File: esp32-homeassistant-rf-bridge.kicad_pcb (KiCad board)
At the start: 2 copper layers, 52 x 51.8 mm, 37 parts, among them J1 USB_C_Receptacle_USB2.0_16P, J2 Conn_02x04_Odd_Even, SW1 SW_Push, SW2 SW_Push, SW3 SW_Push, SW4 SW_Push, U1 ESP32-S2-MINI-1, U2 TSOP41xx, U3 XC6206P332MR, U4 CC1101_E07-M1101D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

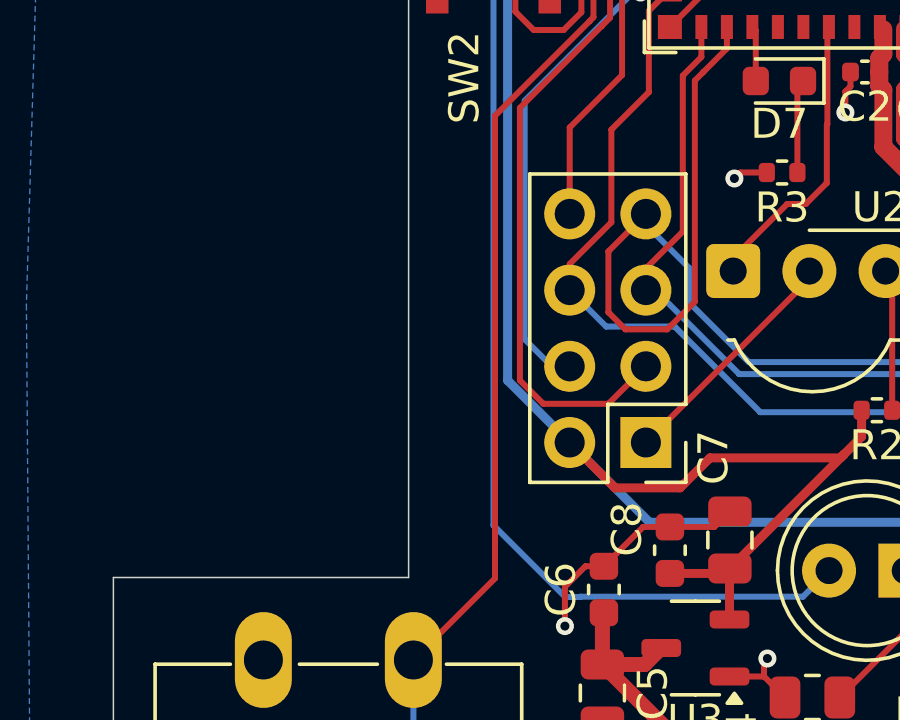
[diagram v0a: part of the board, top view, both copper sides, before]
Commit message: add JLCPCB ID designator
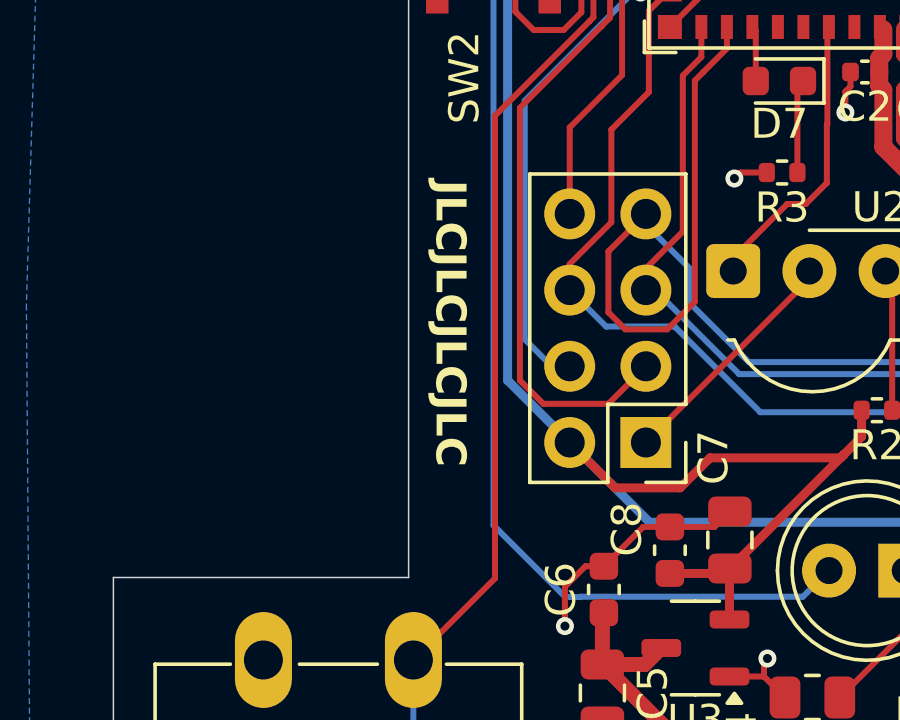
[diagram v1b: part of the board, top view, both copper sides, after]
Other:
- board text added: "JLCJLCJLCJLC"
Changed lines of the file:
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@@
 		(layer "Edge.Cuts")
+	)
+	(gr_text "JLCJLCJLCJLC"
+		(at 87.65 37.75 270)
+		(layer "F.SilkS")
+		(effects
+			(font
+				(size 1 1)
+				(thickness 0.2)
+				(bold yes)
+			)
+			(justify left bottom)
+		)
 	)
 	(gr_text "@grimsteel\n"

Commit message: silkscreen updates, add LDR and mounting holes
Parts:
- added R5: LDR07, OptoDevice:R_LDR_5.0x4.1mm_P3mm_Vertical, F.Cu at (112.0, 52.2)
- added R6: 10K, Resistor_SMD:R_0402_1005Metric, F.Cu at (109.5, 55.3)
- added REF**: MountingHole_3.2mm_M3, MountingHole:MountingHole_3.2mm_M3, F.Cu at (123.7, 48.2)
- added REF**: MountingHole_3.2mm_M3, MountingHole:MountingHole_3.2mm_M3, F.Cu at (82.2, 48.2)
- D6: value D6 -> LD271
- moved QR***** 1.01 mm to (100.5, 28.1)
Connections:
- U1 pad 32: unconnected-(U1-GPIO36-Pad32) -> LDR
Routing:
- net LDR: track 0.00 -> 34.6 mm, vias 0 -> 1
- net +3.3V: track 113.4 -> 117.7 mm
- net GND: track 105.9 -> 106.8 mm, vias 24 -> 25
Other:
- outline, holes or cut-outs redrawn
- board text added: "01/25"
- board text removed: "12/24"

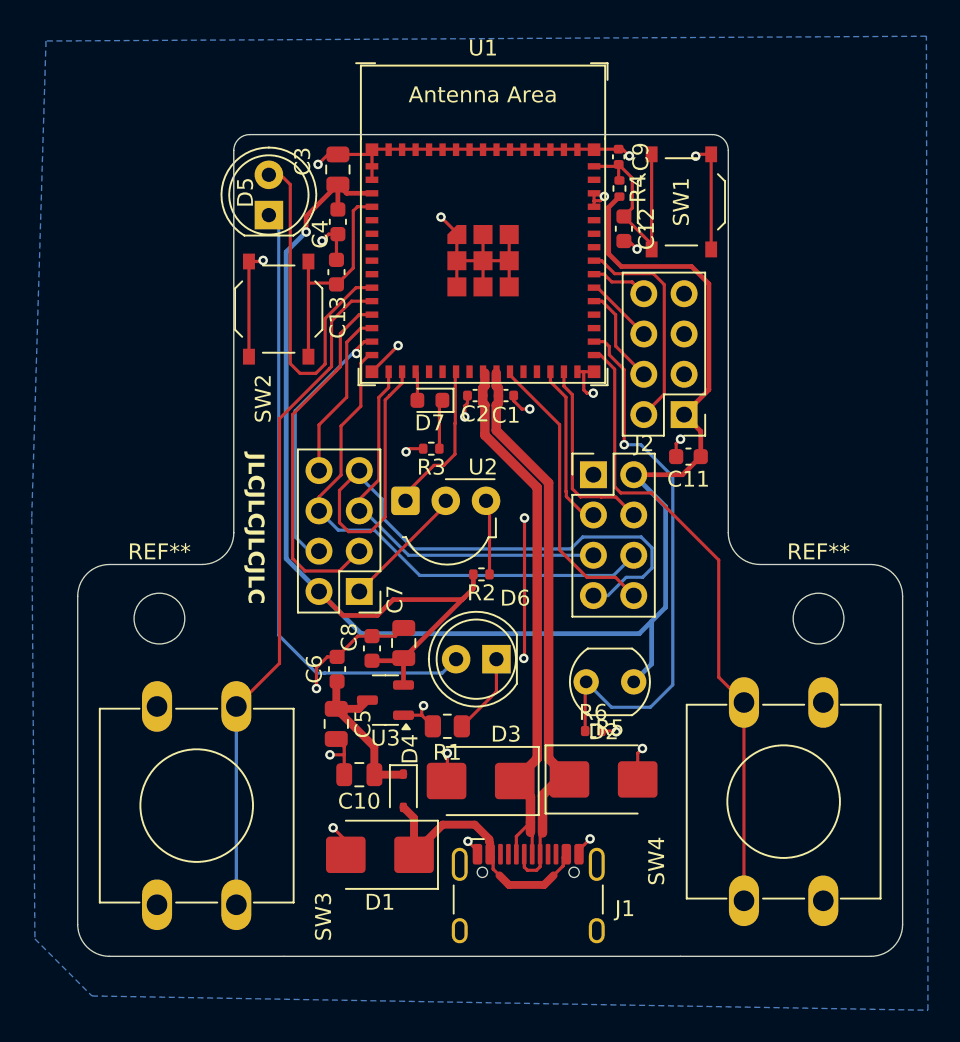
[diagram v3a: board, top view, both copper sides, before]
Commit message: make board smaller, remove problematic components
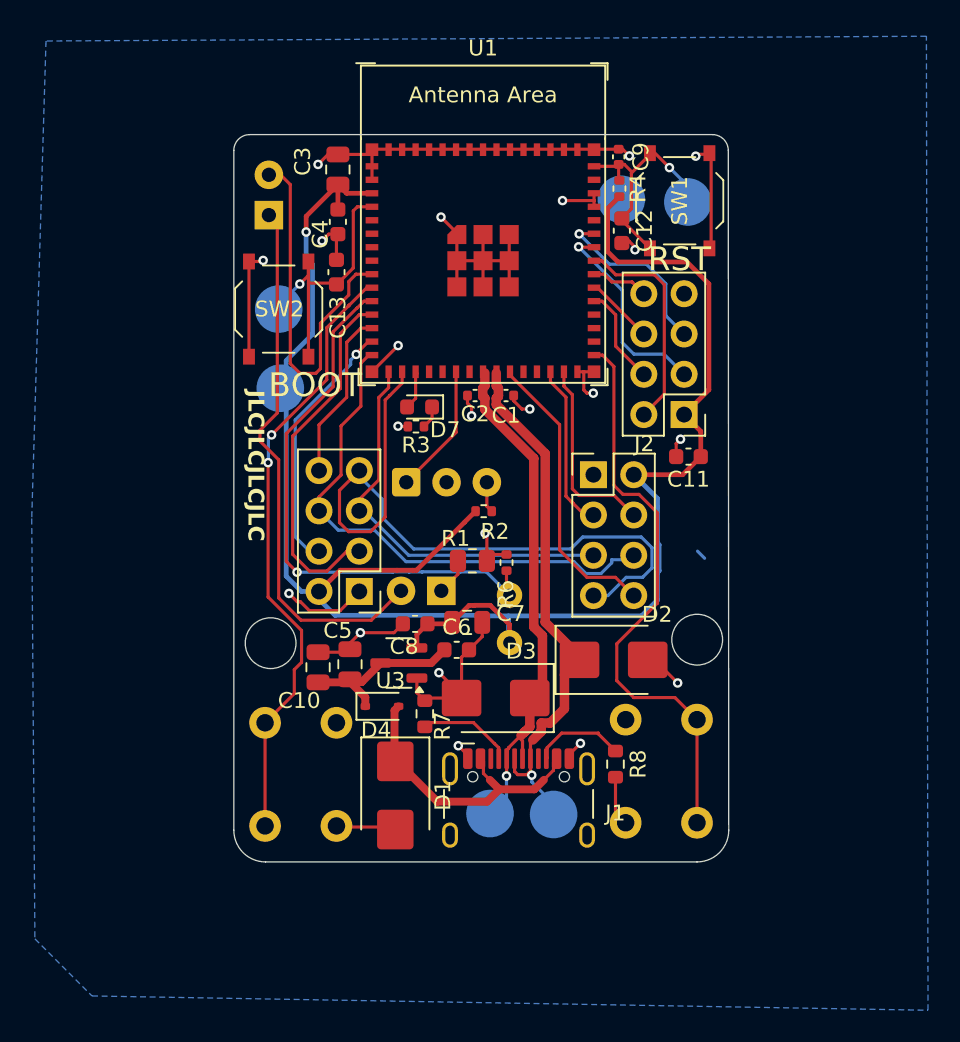
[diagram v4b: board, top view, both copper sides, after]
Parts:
- added R7: 5.1K, Resistor_SMD:R_0603_1608Metric, F.Cu at (98.9, 54.2)
- added R8: 5.1K, Resistor_SMD:R_0603_1608Metric, F.Cu at (110.9, 57.4)
- added TP1: 3V3, TestPoint:TestPoint_Pad_D3.0mm, B.Cu at (89.8, 33.7)
- added TP2: GND, TestPoint:TestPoint_Pad_D3.0mm, B.Cu at (111.3, 21.8)
- added TP3: EN, TestPoint:TestPoint_Pad_D3.0mm, B.Cu at (115.5, 21.9)
- added TP4: BOOT, TestPoint:TestPoint_Pad_D3.0mm, B.Cu at (89.7, 28.7)
- added TP5: D+, TestPoint:TestPoint_Pad_D3.0mm, B.Cu at (107.0, 60.6)
- added TP6: D-, TestPoint:TestPoint_Pad_D3.0mm, B.Cu at (103.0, 60.5)
- D5, D6, REF** (x2), U2: moved to B.Cu
- LDR07: renamed from R5; value LDR07 -> ~; moved to B.Cu
- SW3, SW4: footprint Button_Switch_THT:SW_PUSH-12mm -> Button_Switch_THT:SW_PUSH_6mm; moved to B.Cu
- moved G*** 21.6 mm to (97.3, 58.1)
- moved R6 11.9 mm to (104.0, 44.7), turned to 90 degrees
- moved R1 10.5 mm to (101.9, 44.6), turned to 0 degrees
- moved LDR07 8.21 mm to (104.2, 49.7), turned to 90 degrees
- moved REF** 7.76 mm to (116.0, 49.5)
- moved C6 7.64 mm to (100.9, 50.2), turned to 0 degrees
- moved D2 7.57 mm to (110.8, 50.8)
- moved C10 7.25 mm to (92.2, 51.3), turned to 90 degrees
- moved REF** 7.18 mm to (89.2, 49.8)
- moved J1 6.06 mm to (104.8, 60.8)
- moved SW4 5.74 mm to (116.0, 61.1)
- moved D6 5.54 mm to (99.9, 46.5)
- moved D4 5.49 mm to (96.2, 53.7), turned to 0 degrees
- moved D3 5.32 mm to (103.3, 53.2)
- moved C7 4.21 mm to (101.5, 48.5), turned to 0 degrees
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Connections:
- J1 pad A5: unconnected-(J1-CC1-PadA5) -> Net-(J1-CC1)
- J1 pad B5: unconnected-(J1-CC2-PadB5) -> Net-(J1-CC2)
- J2 pad 3: GND -> TX
- J2 pad 5: GND -> RX
- U1 pad 10: IR LED -> BTN1
- U1 pad 11: BTN1 -> LDR
- U1 pad 32: LDR -> unconnected-(U1-GPIO36-Pad32)
- U1 pad 39: unconnected-(U1-GPIO43/U0TXD/PROG-Pad39) -> TX
- U1 pad 40: unconnected-(U1-GPIO44/U0RXD/PROG-Pad40) -> RX
- U1 pad 9: unconnected-(U1-GPIO5/ADC1_CH4-Pad9) -> IR LED
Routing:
- net TX: track 0.00 -> 12.9 mm, vias 0 -> 1
- net RX: track 0.00 -> 11.4 mm, vias 0 -> 1
- net Net-(J1-CC1): track 0.00 -> 6.66 mm
- net Net-(J1-CC2): track 0.00 -> 5.90 mm
- net Net-(D5-K): track 39.3 -> 34.4 mm
- net BOOT: track 14.2 -> 18.0 mm, vias 0 -> 1
- net D-: track 35.2 -> 31.8 mm, vias 0 -> 1
- net +3.3V: track 117.7 -> 114.4 mm
- net BTN2: track 39.7 -> 36.7 mm
- net BTN1: track 42.3 -> 39.4 mm, vias 0 -> 2
- net Net-(D6-K): track 5.13 -> 2.32 mm
- net Net-(U2-Vs): track 4.73 -> 1.95 mm
- net D+: track 36.5 -> 34.8 mm, vias 0 -> 1
- net Net-(D7-K): track 3.13 -> 1.44 mm
- net IR RECEIVER: track 9.82 -> 8.27 mm
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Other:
- board size 52 x 51.8 mm -> 31.2 x 45.8 mm
- board text added: "BOOT"
- board text added: "D+ D-"
- board text added: "Home Assistant"
- board text added: "RF Bridge"
- board text added: "RST"
- board text added: "RX"
- board text added: "TX"
- board text added: "UART"
- board text removed: "Home Assistant RF Bridge"
- board text removed: "github.com/grimsteel/homeassistant-rf-bridge"

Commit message: use ams1117
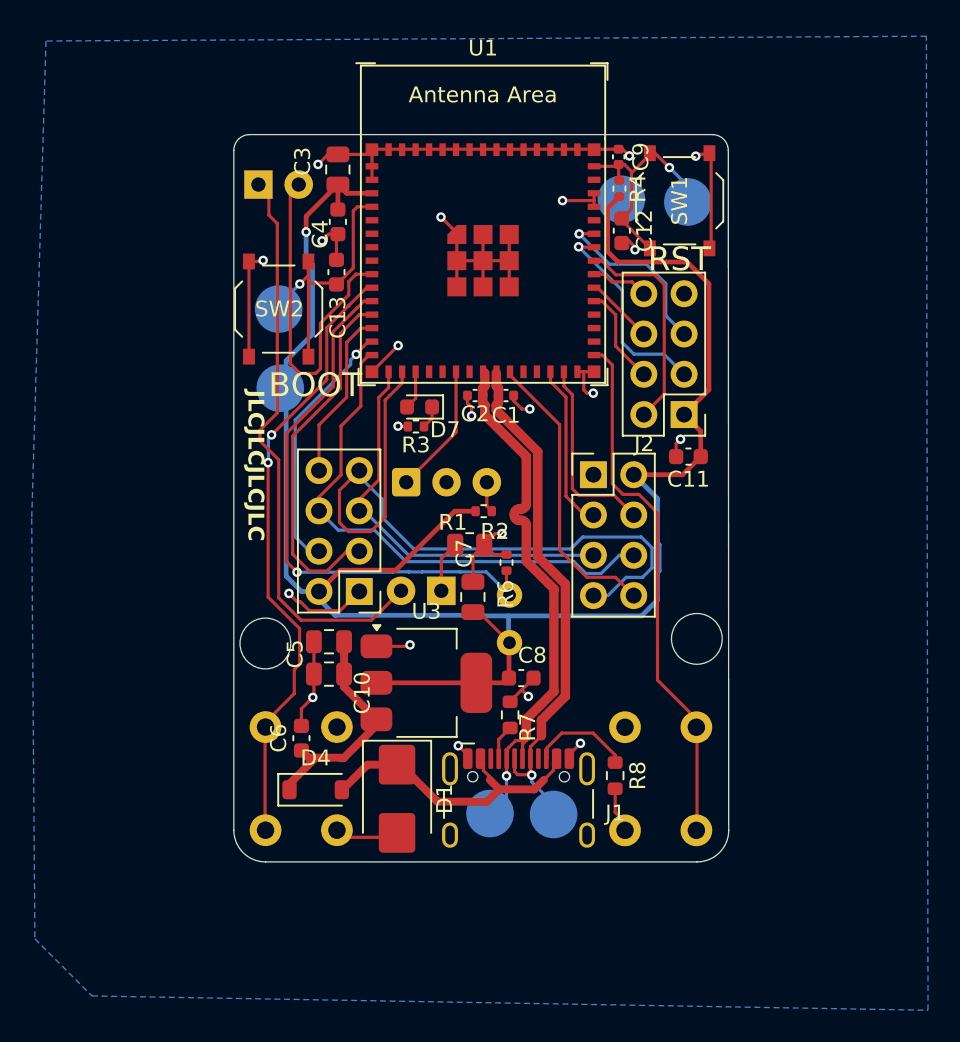
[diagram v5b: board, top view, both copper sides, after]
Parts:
- removed D2, D3: P6SMB6.8CA/TR13, Diode_SMD:D_SMB
- D4: footprint Diode_SMD:D_SOD-323 -> Diode_SMD:D_SOD-123
- U3: value XC6206P332MR -> AMS1117-3.3; footprint Package_TO_SOT_SMD:SOT-23-3 -> Package_TO_SOT_SMD:SOT-223-3_TabPin2
- moved C6 11.3 mm to (91.1, 55.8), turned to 90 degrees
- moved G*** 11.0 mm to (108.0, 55.7)
- moved C8 7.51 mm to (105.0, 52.0), turned to 0 degrees
- moved D4 6.72 mm to (92.0, 59.0)
- moved R7 5.38 mm to (104.3, 54.3)
- moved U3 2.14 mm to (99.0, 52.3), turned to 0 degrees
- moved D5 2.03 mm to (88.4, 20.9), turned to 0 degrees
- moved C5 1.94 mm to (92.8, 49.7), turned to 180 degrees
- moved C7 1.64 mm to (101.9, 46.9), turned to 90 degrees
- moved R1 1.02 mm to (101.7, 43.6)
- moved C10 0.81 mm to (92.8, 51.7), turned to 180 degrees
- moved R8 0.73 mm to (110.9, 58.1)
- moved SW4 0.48 mm to (116.0, 61.6)
- moved REF** 0.33 mm to (88.8, 49.8)
- moved SW3 0.27 mm to (88.8, 55.0)
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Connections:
- U1 pad 32: unconnected-(U1-GPIO36-Pad32) -> BUZ
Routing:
- net GND: track 106.7 -> 98.2 mm
- net +3.3V: track 114.4 -> 119.0 mm
- net Net-(J1-CC1): track 6.66 -> 2.23 mm
- net +5V: track 10.7 -> 14.6 mm
- net BTN2: track 36.7 -> 33.1 mm
- net D-: track 31.8 -> 34.0 mm
- net Net-(D5-K): track 34.4 -> 36.6 mm
- net IR LED: track 23.1 -> 21.7 mm
- net D+: track 34.8 -> 33.5 mm
- net Net-(D6-K): track 2.32 -> 3.26 mm
- net VBUS: track 18.6 -> 19.5 mm
- net BTN1: track 39.4 -> 38.8 mm
- net Net-(J1-CC2): track 5.90 -> 6.42 mm
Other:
- board text added: "03/25"
- board text removed: "01/25"

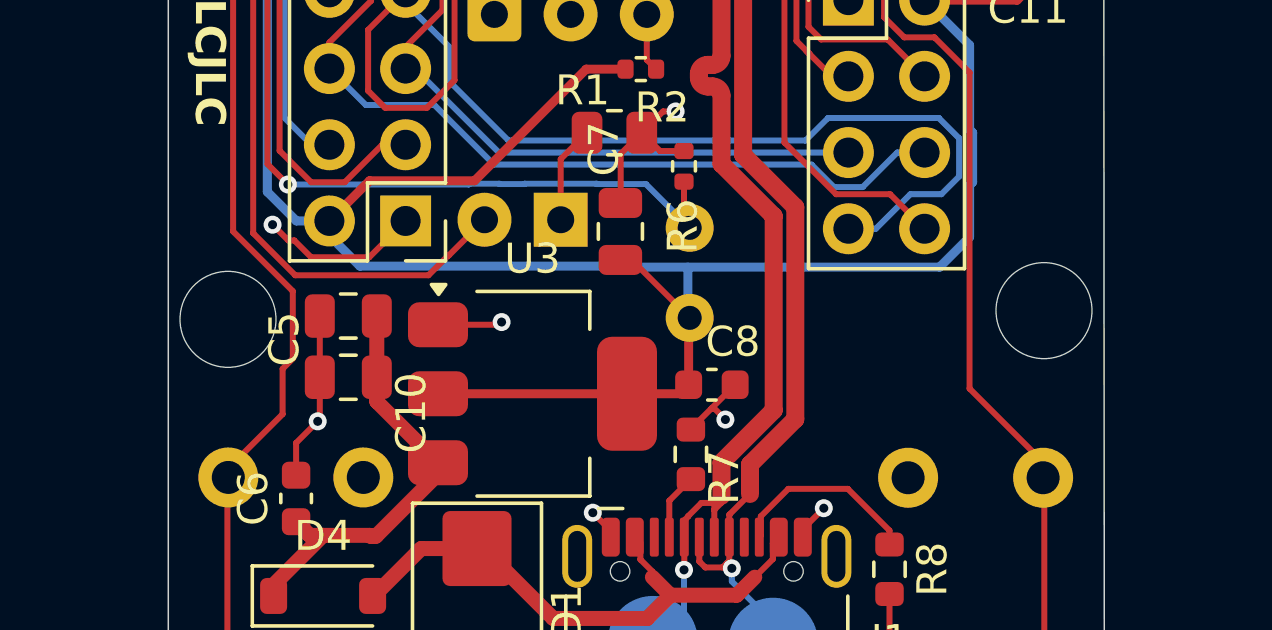
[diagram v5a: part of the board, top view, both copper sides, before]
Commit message: reduce mounting point size
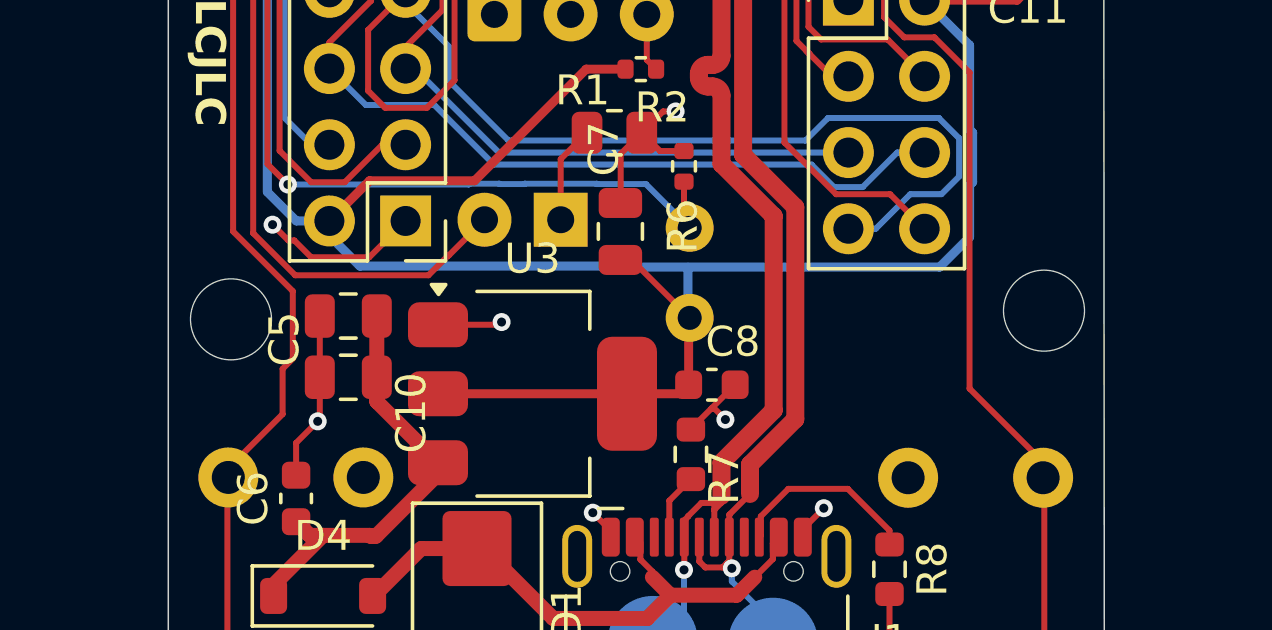
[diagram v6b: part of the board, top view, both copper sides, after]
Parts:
- REF** (x2): value MountingHole_3.2mm_M3 -> MountingHole_2.7mm_M2.5; footprint MountingHole:MountingHole_3.2mm_M3 -> MountingHole:MountingHole_2.7mm_M2.5
- moved REF** 0.10 mm to (88.9, 49.8)
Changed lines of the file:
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@@
 			(psa4output no)
 			(plot_black_and_white yes)
-			(plotinvisibletext no)
 			(sketchpadsonfab no)
 			(plotpadnumbers no)
@@
 		)
 	)
-	(footprint "MountingHole:MountingHole_3.2mm_M3"
+	(footprint "MountingHole:MountingHole_2.7mm_M2.5"
 		(layer "B.Cu")
 		(at 116.03 49.49)
-		(descr "Mounting Hole 3.2mm, no annular, M3")
-		(tags "mounting hole 3.2mm no annular m3")
+		(descr "Mounting Hole 2.7mm, M2.5, no annular, generated by kicad-footprint-generator mountinghole.py")
+		(tags "mountinghole M2.5")
 		(property "Reference" "REF**"
-			(at 0 4.2 180)
+			(at 0 3.65 180)
 			(layer "B.SilkS")
-			(hide yes)
 			(effects
 				(font
@@
 			)
 		)
-		(property "Value" "MountingHole_3.2mm_M3"
-			(at 0 -4.2 180)
+		(property "Value" "MountingHole_2.7mm_M2.5"
+			(at 0 -3.65 180)
 			(layer "B.Fab")
 			(effects
@@
 		(property "Datasheet" ""
 			(at 0 0 180)
-			(unlocked yes)
 			(layer "B.Fab")
 			(hide yes)
@@
 		(property "Description" ""
 			(at 0 0 180)
-			(unlocked yes)
 			(layer "B.Fab")
 			(hide yes)
@@
 			)
 		)
-		(attr board_only exclude_from_pos_files exclude_from_bom)
+		(attr exclude_from_pos_files exclude_from_bom)
 		(fp_circle
 			(center 0 0)
-			(end 3.2 0)
+			(end 2.7 0)
 			(stroke
 				(width 0.15)
@@
 		(fp_circle
 			(center 0 0)
-			(end 3.45 0)
+			(end 2.95 0)
 			(stroke
 				(width 0.05)
@@
 		(pad "" np_thru_hole circle
 			(at 0 0)
-			(size 3.2 3.2)
-			(drill 3.2)
+			(size 2.7 2.7)
+			(drill 2.7)
 			(layers "*.Cu" "*.Mask")
 		)
@@
 		(embedded_fonts no)
 	)
-	(footprint "MountingHole:MountingHole_3.2mm_M3"
+	(footprint "MountingHole:MountingHole_2.7mm_M2.5"
 		(layer "B.Cu")
-		(at 88.83 49.78)
-		(descr "Mounting Hole 3.2mm, no annular, M3")
-		(tags "mounting hole 3.2mm no annular m3")
+		(at 88.93 49.78)
+		(descr "Mounting Hole 2.7mm, M2.5, no annular, generated by kicad-footprint-generator mountinghole.py")
+		(tags "mountinghole M2.5")
 		(property "Reference" "REF**"
-			(at 0 4.2 180)
+			(at 0 3.65 180)
 			(layer "B.SilkS")
-			(hide yes)
 			(effects
 				(font
@@
 			)
 		)
-		(property "Value" "MountingHole_3.2mm_M3"
-			(at 0 -4.2 180)
+		(property "Value" "MountingHole_2.7mm_M2.5"
+			(at 0 -3.65 180)
 			(layer "B.Fab")
 			(effects
@@
 		(property "Datasheet" ""
 			(at 0 0 180)
-			(unlocked yes)
 			(layer "B.Fab")
 			(hide yes)
@@
 		(property "Description" ""
 			(at 0 0 180)
-			(unlocked yes)
 			(layer "B.Fab")
 			(hide yes)
@@
 			)
 		)
-		(attr board_only exclude_from_pos_files exclude_from_bom)
+		(attr exclude_from_pos_files exclude_from_bom)
 		(fp_circle
 			(center 0 0)
-			(end 3.2 0)
+			(end 2.7 0)
 			(stroke
 				(width 0.15)
@@
 		(fp_circle
 			(center 0 0)
-			(end 3.45 0)
+			(end 2.95 0)
 			(stroke
 				(width 0.05)
@@
 		(pad "" np_thru_hole circle
 			(at 0 0)
-			(size 3.2 3.2)
-			(drill 3.2)
+			(size 2.7 2.7)
+			(drill 2.7)
 			(layers "*.Cu" "*.Mask")
 		)
